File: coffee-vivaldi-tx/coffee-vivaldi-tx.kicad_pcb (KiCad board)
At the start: 2 copper layers, 40 parts, among them U1 MAX2750AUA+, U2 SE2565T-R, U3 SMA_PCB_Edge_Mount, U4 SMA_PCB_Edge_Mount

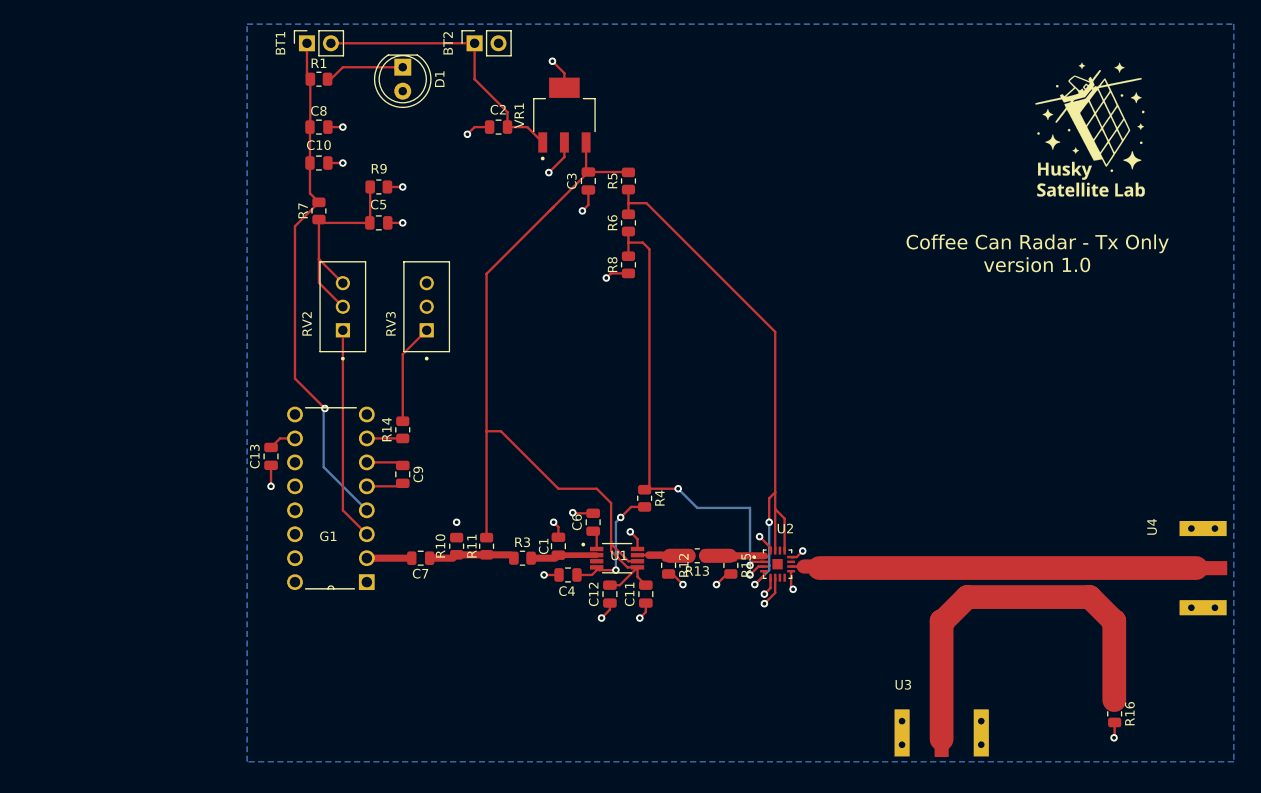
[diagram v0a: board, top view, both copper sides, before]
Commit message: Tx test board version 1
Components chosen, board ready for review
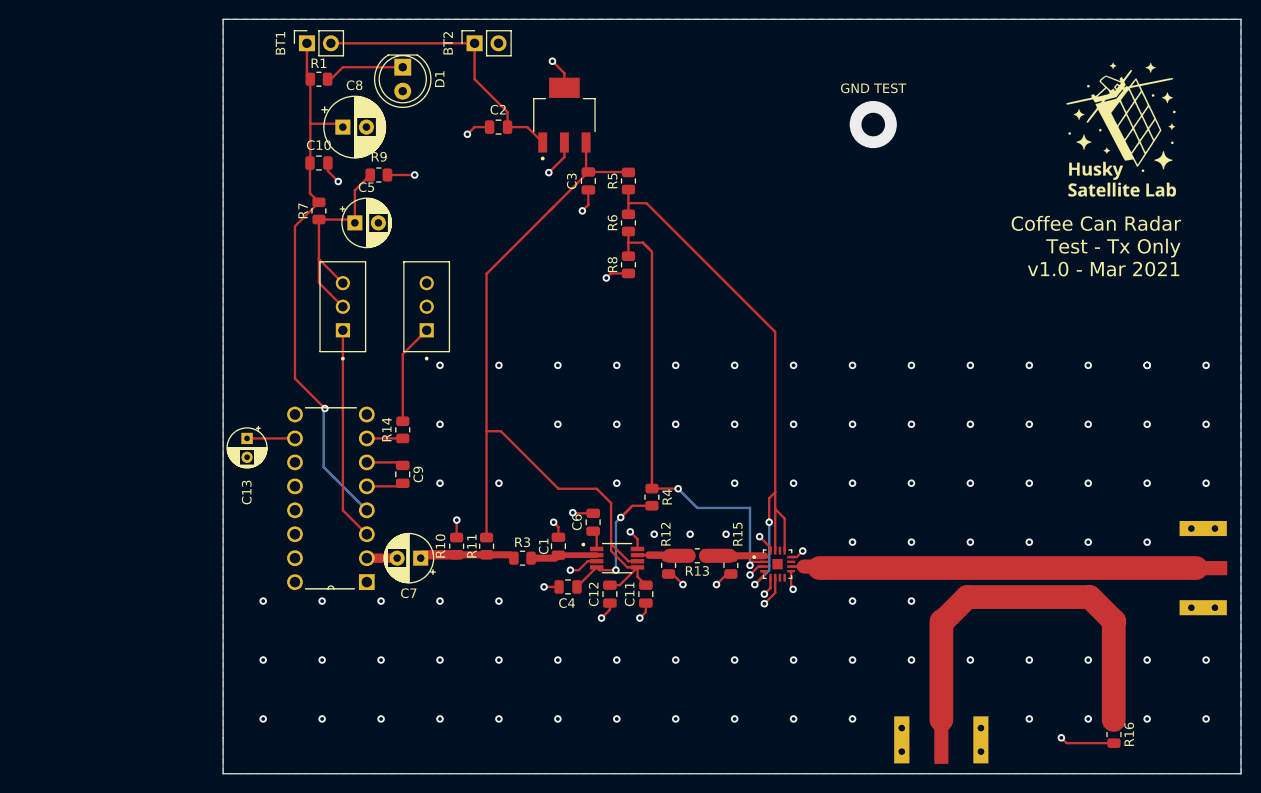
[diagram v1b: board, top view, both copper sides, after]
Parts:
- C13: footprint Capacitor_SMD:C_0805_2012Metric -> Capacitor_THT:CP_Radial_D4.0mm_P2.00mm
- C5, C7: footprint Capacitor_SMD:C_0805_2012Metric -> Capacitor_THT:CP_Radial_D5.0mm_P2.50mm
- C8: footprint Capacitor_SMD:C_0805_2012Metric -> Capacitor_THT:CP_Radial_D6.3mm_P2.50mm
- moved G*** 3.30 mm to (222.2, 62.5)
- moved C13 3.18 mm to (129.5, 95.2), turned to 270 degrees
- moved C5 2.54 mm to (141.0, 72.4), turned to 0 degrees
- moved C8 2.54 mm to (139.7, 62.2)
- moved R16 2.20 mm to (221.5, 126.7)
- moved C4 1.27 mm to (163.6, 111.0)
- moved R9 1.27 mm to (143.5, 67.3)
- moved R4 0.78 mm to (172.5, 101.5)
- moved U3 0.73 mm to (203.2, 127.0)
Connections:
- C11 pad 2: Net-(R12-Pad1) -> 5V_OUT
- C12 pad 2: Net-(R12-Pad1) -> 5V_OUT
- C13 pad 1: GND -> Net-(C13-Pad1)
- C13 pad 2: Net-(C13-Pad2) -> GND
- C3 pad 1: Net-(R12-Pad1) -> 5V_OUT
- C5 pad 1: GND -> Net-(C5-Pad1)
- C5 pad 2: Net-(C5-Pad2) -> GND
- G1 pad 10: Net-(C13-Pad2) -> Net-(C13-Pad1)
- R11 pad 1: Net-(R12-Pad1) -> 5V_OUT
- R5 pad 2: Net-(R12-Pad1) -> 5V_OUT
- R7 pad 1: Net-(C5-Pad2) -> Net-(C5-Pad1)
- R9 pad 2: Net-(C5-Pad2) -> Net-(C5-Pad1)
- RV2 pad 2: Net-(C5-Pad2) -> Net-(C5-Pad1)
- RV2 pad 3: Net-(C5-Pad2) -> Net-(C5-Pad1)
- U1 pad 5: Net-(R12-Pad1) -> 5V_OUT
- U1 pad 6: Net-(R12-Pad1) -> 5V_OUT
- U1 pad 8: Net-(R12-Pad1) -> GND
- VR1 pad 3: Net-(R12-Pad1) -> 5V_OUT
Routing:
- net Net-(R12-Pad1): track 94.1 -> 5.59 mm, vias 1 -> 0
- net 5V_OUT: track 0.00 -> 86.4 mm
- net Net-(C5-Pad1): track 0.00 -> 24.1 mm
- net Net-(C5-Pad2): track 23.3 -> 0.00 mm
- net GND: track 51.1 -> 59.2 mm, vias 24 -> 113
- net Net-(C13-Pad1): track 0.00 -> 5.08 mm
- net 12V_OUT: track 54.4 -> 58.0 mm
- net Net-(C13-Pad2): track 2.94 -> 0.00 mm
- net Net-(C4-Pad2): track 13.6 -> 16.3 mm
- net RAMP_SIGNAL: track 9.23 -> 11.0 mm
- net Net-(C7-Pad2): track 4.76 -> 3.22 mm
- net (no net): vias 1 -> 0
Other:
- board outline added: 107.9 x 80 mm
- board text added: "Coffee Can Radar Test - Tx Only v1.0 - Mar 2021"
- board text added: "GND TEST"
- board text removed: "Coffee Can Radar - Tx Only version 1.0"

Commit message: Small edit to Tx PCB
Smaller area to save space and money :)
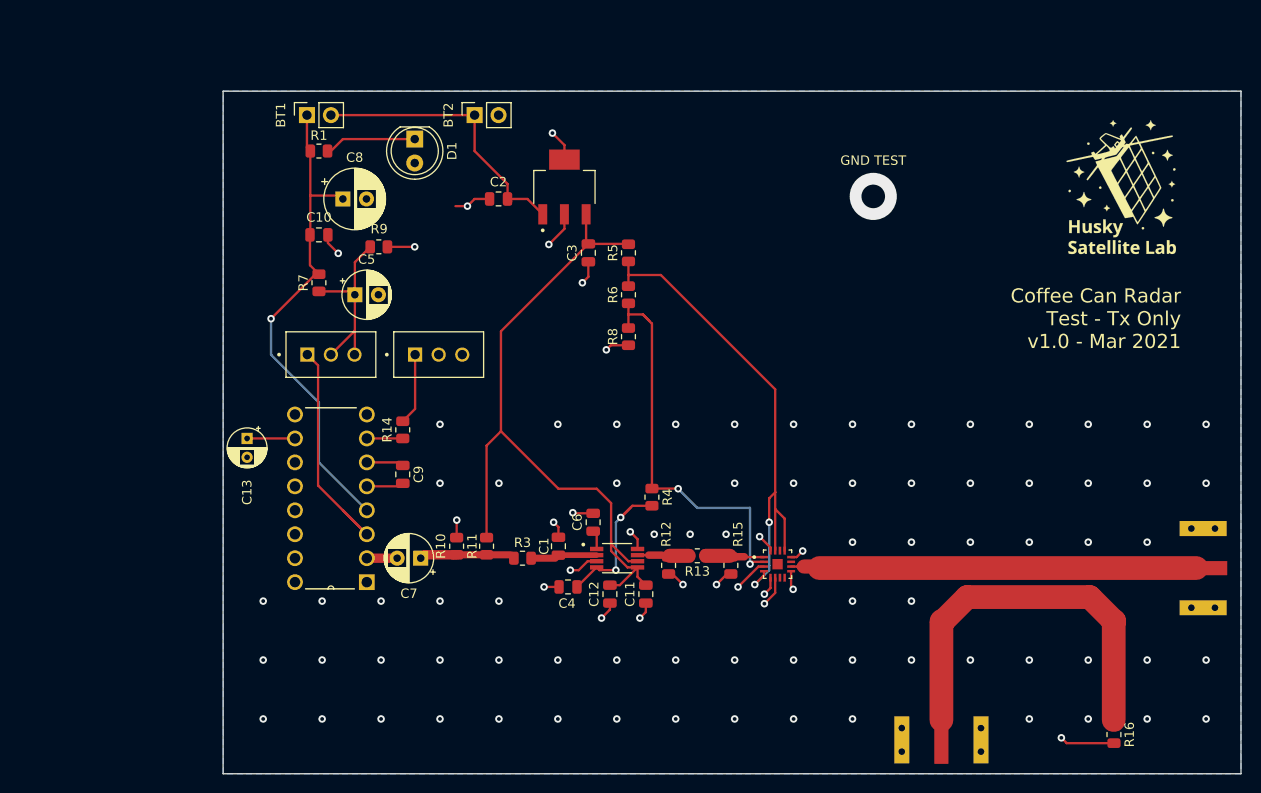
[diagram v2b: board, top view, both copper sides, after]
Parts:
- moved D1 7.73 mm to (147.3, 63.5)
- moved C3 7.62 mm to (165.7, 75.6)
- moved C5 7.62 mm to (141.0, 80.0)
- moved R5 7.62 mm to (170.0, 75.6)
- moved R6 7.62 mm to (170.0, 80.0)
- moved R8 7.62 mm to (170.0, 84.5)
- moved R9 7.62 mm to (143.5, 74.9)
- moved BT1 7.62 mm to (135.9, 61.0)
- moved BT2 7.62 mm to (153.7, 61.0)
- moved C2 7.62 mm to (156.2, 69.8)
- moved C8 7.62 mm to (139.7, 69.8)
- moved R1 7.62 mm to (137.2, 64.8)
- moved VR1 7.62 mm to (163.2, 68.6)
- moved C10 7.62 mm to (137.2, 73.7)
- moved R7 7.62 mm to (137.2, 78.7)
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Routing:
- net 5V_OUT: track 86.4 -> 76.6 mm
- net 3.6V_OUT: track 50.4 -> 42.8 mm
- net 4V_OUT: track 64.4 -> 57.7 mm
- net 12V_OUT: track 58.0 -> 52.6 mm
- net Net-(C5-Pad1): track 24.1 -> 20.2 mm
- net Net-(R14-Pad2): track 10.7 -> 7.61 mm
- net GND: track 59.2 -> 62.2 mm, vias 113 -> 98
- net Net-(G1-Pad3): track 22.7 -> 25.3 mm
- net Net-(D1-Pad1): track 8.50 -> 9.77 mm
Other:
- board size 107.9 x 80 mm -> 107.9 x 72.4 mm

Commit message: Edited PCB dimensions, added gerber files
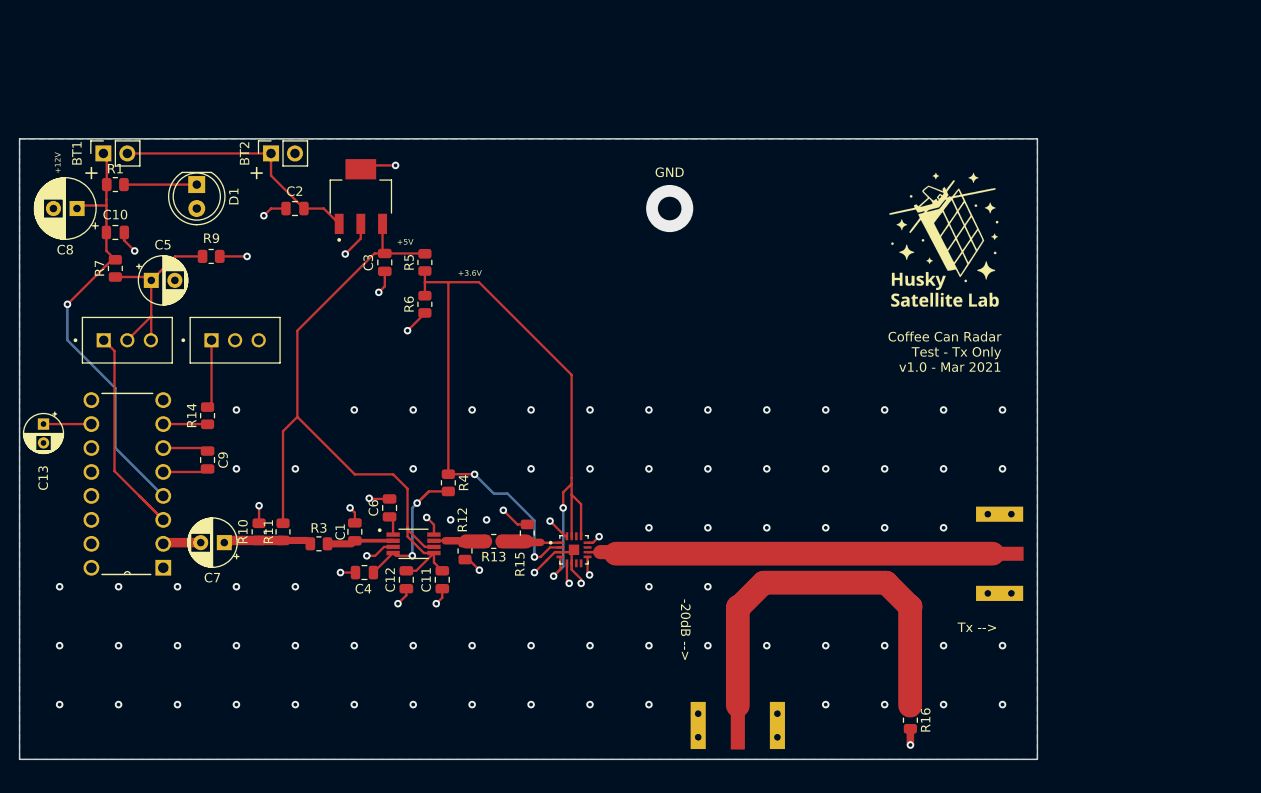
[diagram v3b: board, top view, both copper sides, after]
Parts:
- removed R8: 15k, Resistor_SMD:R_0805_2012Metric
- R5: value 4.12k -> 3.83K
- R6: value 1.69k -> 10K
- moved C8 28.2 mm to (111.5, 70.9), turned to 180 degrees
- moved D1 23.6 mm to (124.2, 68.3)
- moved BT1 22.0 mm to (114.3, 65.0)
- moved BT2 22.0 mm to (132.1, 65.0)
- moved R1 21.9 mm to (115.6, 68.3)
- moved R15 21.9 mm to (159.3, 105.3), turned to 90 degrees
- moved C1 21.6 mm to (141.0, 105.2)
- moved C4 21.6 mm to (142.0, 109.5)
- moved C5 21.6 mm to (119.4, 78.5)
- moved C6 21.6 mm to (144.7, 102.6)
- moved G1 21.6 mm to (113.0, 91.2)
- moved R11 21.6 mm to (133.3, 105.2)
- moved R12 21.6 mm to (152.7, 107.2)
- moved R13 21.6 mm to (155.7, 106.2)
- moved R16 21.6 mm to (199.9, 125.1)
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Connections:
- R5 pad 1: 4V_OUT -> 3.6V_OUT
- R6 pad 1: 3.6V_OUT -> GND
- R6 pad 2: 4V_OUT -> 3.6V_OUT
- U2 pad 13: 4V_OUT -> 3.6V_OUT
- U2 pad 15: 4V_OUT -> 3.6V_OUT
- U2 pad 17: (no net) -> GND
- U2 pad 4: 4V_OUT -> 3.6V_OUT
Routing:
- net 4V_OUT: track 57.7 -> 0.00 mm, vias 2 -> 0
- net 3.6V_OUT: track 42.8 -> 95.8 mm, vias 2 -> 4
- net 12V_OUT: track 52.6 -> 46.7 mm
- net Net-(BT1-Pad2): track 30.1 -> 27.7 mm
- net 5V_OUT: track 76.6 -> 74.7 mm
- net Net-(D1-Pad1): track 9.77 -> 8.08 mm
- net RAMP_SIGNAL: track 11.0 -> 9.36 mm
- net RF_OUT1: track 44.3 -> 42.8 mm
- net Net-(R12-Pad1): track 5.59 -> 4.63 mm
- net Net-(G1-Pad7): track 3.81 -> 4.71 mm
- net Net-(C9-Pad2): track 3.94 -> 4.83 mm
- net Net-(C9-Pad1): track 3.94 -> 4.83 mm
- net Net-(C7-Pad2): track 3.22 -> 4.03 mm
- net GND: track 62.2 -> 61.5 mm, vias 98 -> 97
- net Net-(C5-Pad1): track 20.2 -> 20.9 mm
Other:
- board size 107.9 x 72.4 mm -> 108 x 65.8 mm
- board text added: "+"
- board text added: "+12V"
- board text added: "+3.6V"
- board text added: "+5V"
- board text added: "-20dB -->"
- board text added: "GND"
- board text added: "Tx -->"
- board text removed: "GND TEST"

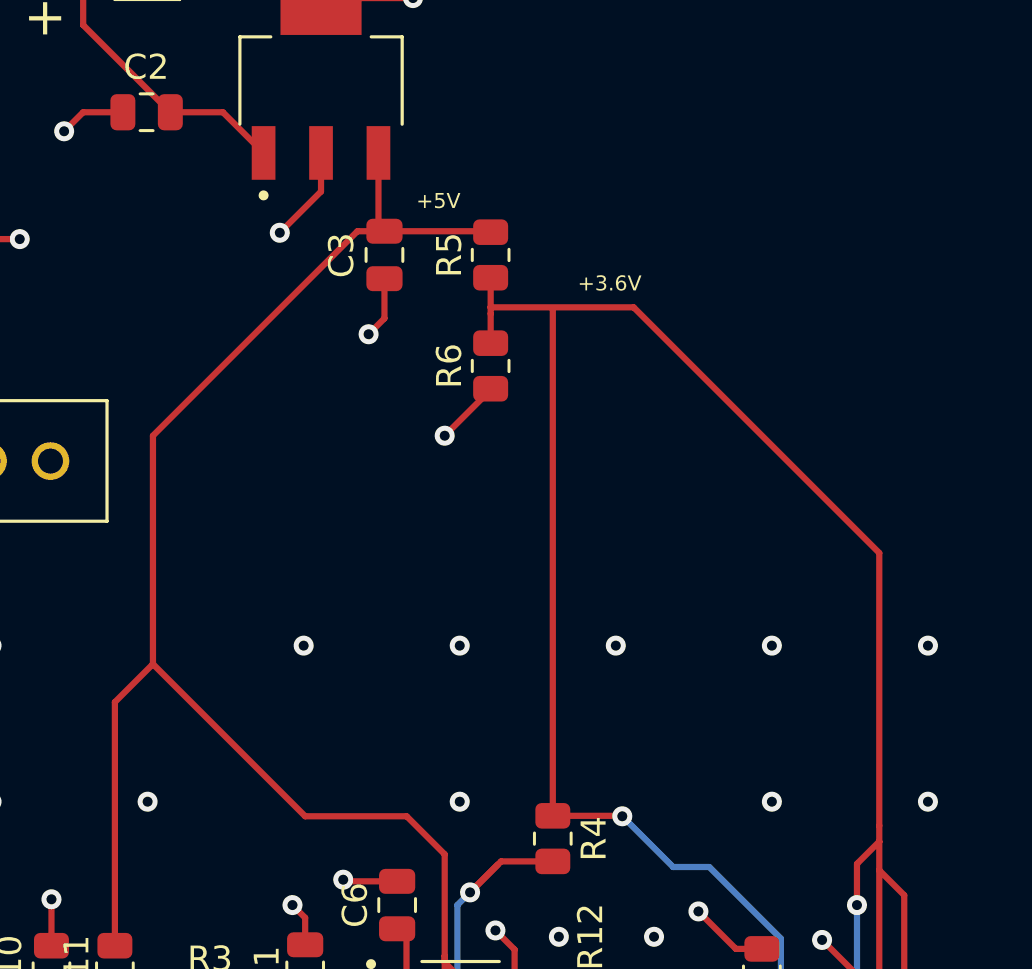
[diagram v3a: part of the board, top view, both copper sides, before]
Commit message: Update schematic and PCB layout
reference for full design
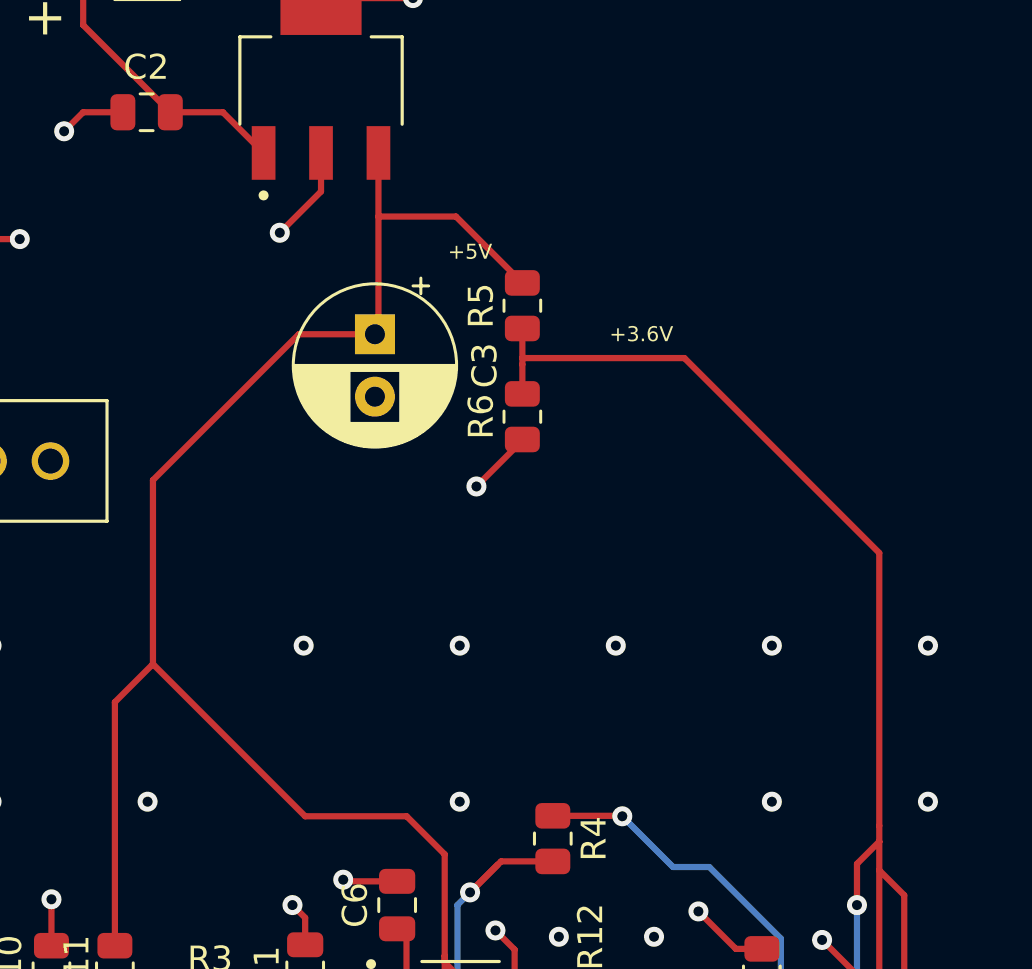
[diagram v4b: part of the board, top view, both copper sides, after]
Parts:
- C3: footprint Capacitor_SMD:C_0805_2012Metric -> Capacitor_THT:CP_Radial_D6.3mm_P2.50mm
- R16: value 50 -> 51
- moved C3 3.20 mm to (143.8, 79.8)
- moved R6 2.40 mm to (149.7, 83.1)
- moved R5 2.40 mm to (149.7, 78.6)
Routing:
- net 3.6V_OUT: track 95.8 -> 73.4 mm
- net 5V_OUT: track 74.7 -> 78.0 mm
- net GND: track 61.5 -> 59.0 mm, vias 97 -> 96
